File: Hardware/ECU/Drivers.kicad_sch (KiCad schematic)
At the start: 52 parts, among them SW4 SW_DPDT_x2, U10 TC4424A, U5 TC4424A, U6 TC4424A, U7 MC33810, U8 MC33810, U9 TC4424A

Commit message: PCB
Platine Vernetzt
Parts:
- removed D10, D12, D14, D16: D, Diode_SMD:D_SOD-323, symbol Device:D
- removed D17, D20, D23, D24, D3, D4, D6, D8: LED, LED_SMD:LED_0805_2012Metric, symbol Device:LED
- removed R11, R12, R14, R16, R19, R22, R25, R26: 1k, Resistor_SMD:R_0805_2012Metric, symbol Device:R
- removed R18: 10k, Resistor_SMD:R_0805_2012Metric, symbol Device:R
- removed U10, U6: TC4424A, Package_SO:SOIC-8_3.9x4.9mm_P1.27mm, symbol IC_Automotive:TC4424A
- removed U8: MC33810, IC_Automotive:SOIC32-P0.65-33N, symbol IC_Automotive:MC33810
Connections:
- net 12V-SW: now also R13.2; no longer R13.1
- net at D5.2 (A): now also R13.1; no longer R13.2
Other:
- moved on the sheet: R13

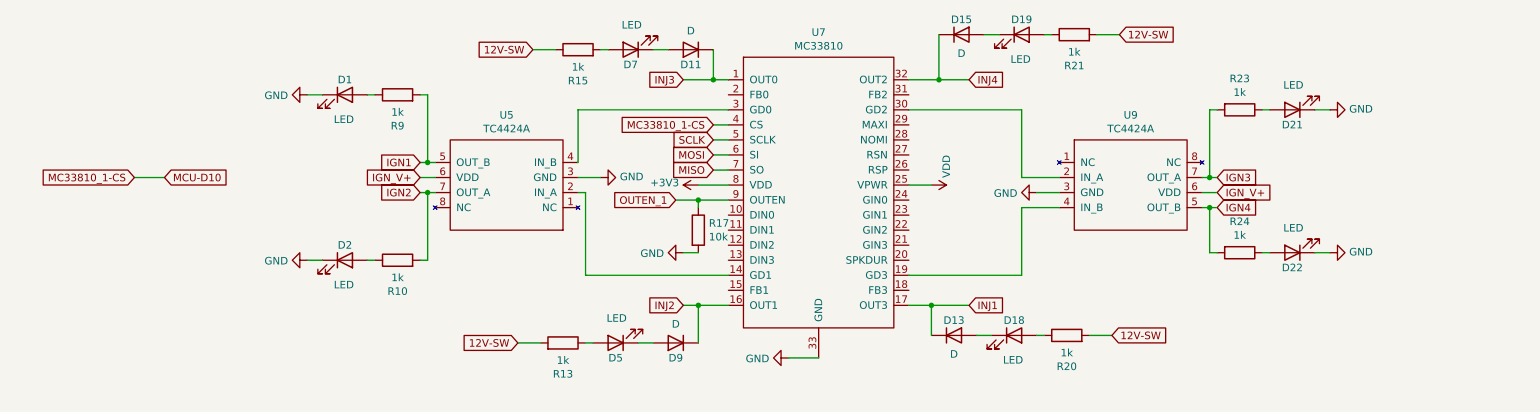
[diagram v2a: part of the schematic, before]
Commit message: Add new footprint for TO-220AB MOSFET (IRFB4110PBF)
- Created a new KiCad module for the TO254P483X1016X1994-3P footprint.
- Included necessary graphical elements such as courtyard, fabrication, and silkscreen layers.
- Defined pads for through-hole connections with appropriate dimensions and drill sizes.
- Added a 3D model reference for the IRFB4110PBF component.
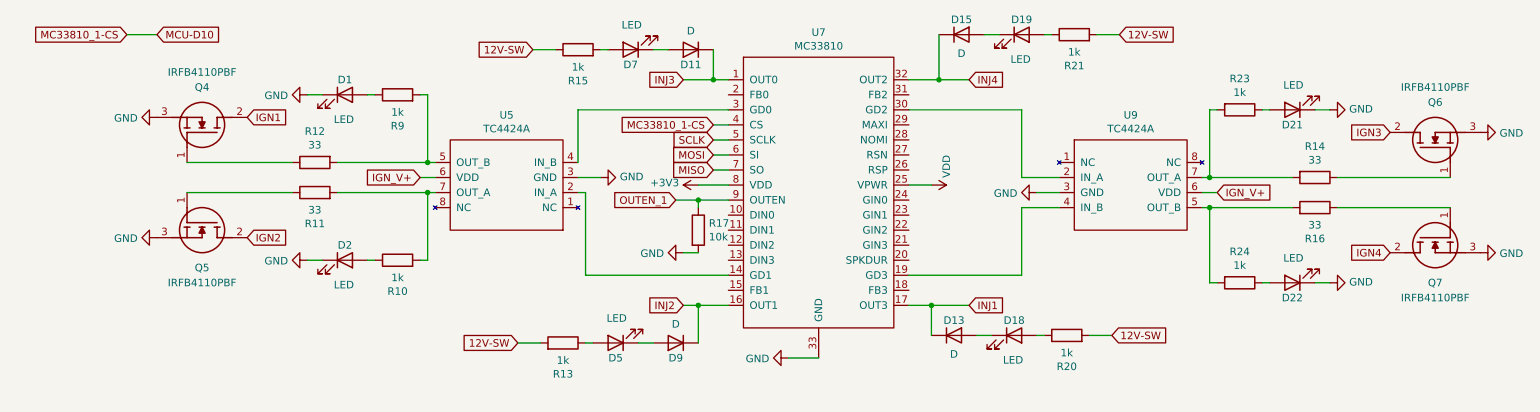
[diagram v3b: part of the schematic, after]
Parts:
- added Q4, Q5, Q6, Q7: IRFB4110PBF, TO254P483X1016X1994-3P, symbol LIB_IRFB4110PBF:IRFB4110PBF
- added R11, R12, R14, R16: 33, Resistor_SMD:R_0805_2012Metric, symbol Device:R
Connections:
- net GND: now also Q4.3 (S), Q5.3 (S), Q6.3 (S), Q7.3 (S)
- net IGN1: now also Q4.2 (D); no longer R9.2, U5.5 (OUT_B)
- net IGN2: now also Q5.2 (D); no longer R10.2, U5.7 (OUT_A)
- net IGN3: now also Q6.2 (D); no longer R23.2, U9.7 (OUT_A)
- net IGN4: now also Q7.2 (D); no longer R24.2, U9.5 (OUT_B)
- new net: R12.2, R9.2, U5.5 (OUT_B)
- new net: Q5.1 (G), R11.1
- new net: Q7.1 (G), R16.1
- new net: R16.2, R24.2, U9.5 (OUT_B)
- new net: R14.2, R23.2, U9.7 (OUT_A)
- new net: R10.2, R11.2, U5.7 (OUT_A)
- new net: Q4.1 (G), R12.1
- new net: Q6.1 (G), R14.1
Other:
- moved on the sheet: D22, R24

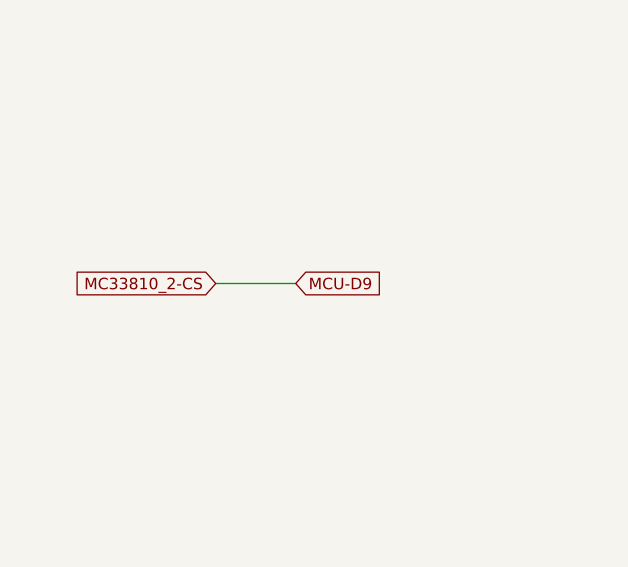
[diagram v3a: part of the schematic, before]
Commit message: modified:   Hardware/ECU/Drivers.kicad_sch 	deleted:    Hardware/ECU/ECU-backups/ECU-2025-05-15_143348.zip 	deleted:    Hardware/ECU/ECU-backups/ECU-2025-05-15_144355.zip 	deleted:    Hardware/ECU/ECU-backups/ECU-2025-05-15_152109.zip 	deleted:    Hardware/ECU/ECU-backups/ECU-2025-05-15_161628.zip 	deleted:    Hardware/ECU/ECU-backups/ECU-2025-05-15_162311.zip 	deleted:    Hardware/ECU/ECU-backups/ECU-2025-05-16_191516.zip 	deleted:    Hardware/ECU/ECU-backups/ECU-2025-05-16_192518.zip 	deleted:    Hardware/ECU/ECU-backups/ECU-2025-05-16_193610.zip 	new file:   Hardware/ECU/ECU-backups/ECU-2025-05-20_084251.zip 	new file:   Hardware/ECU/ECU-backups/ECU-2025-05-20_085713.zip 	new file:   Hardware/ECU/ECU-backups/ECU-2025-05-20_090304.zip 	new file:   Hardware/ECU/ECU-backups/ECU-2025-05-20_142748.zip 	new file:   Hardware/ECU/ECU-backups/ECU-2025-05-20_150003.zip 	new file:   Hardware/ECU/ECU-backups/ECU-2025-05-27_131057.zip 	new file:   Hardware/ECU/ECU-backups/ECU-2025-05-27_141528.zip 	new file:   Hardware/ECU/ECU-backups/ECU-2025-05-27_154948.zip 	new file:   Hardware/ECU/ECU-backups/ECU-2025-05-27_155558.zip 	new file:   Hardware/ECU/ECU.csv 	modified:   Hardware/ECU/ECU.kicad_pcb 	modified:   Hardware/ECU/ECU.kicad_pcb.zip 	new file:   Hardware/ECU/ECU.xml 	modified:   Hardware/ECU/Power-Regulator.kicad_sch 	modified:   Hardware/ECU/docs/Pinout.ods 	modified:   Hardware/ECU/fp-info-cache 	modified:   Hardware/ECU/fp-lib-table 	new file:   Hardware/ECU/lib/CRCW060349K9FKEAC.step 	new file:   Hardware/ECU/lib/CRCW060349K9FKEAC.wrl 	new file:   Hardware/ECU/lib/GRM21BC81A226ME44L.step 	new file:   Hardware/ECU/lib/GRM21BC81A226ME44L.wrl 	new file:   Hardware/ECU/lib/SamacSys_Parts.3dshapes/NE555DR.stp 	new file:   Hardware/ECU/lib/SamacSys_Parts.dcm 	new file:   Hardware/ECU/lib/SamacSys_Parts.kicad_sym 	new file:   Hardware/ECU/lib/SamacSys_Parts.lib 	new file:   Hardware/ECU/lib/SamacSys_Parts.mod 	new file:   Hardware/ECU/lib/SamacSys_Parts.pretty/NE555DR.kica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
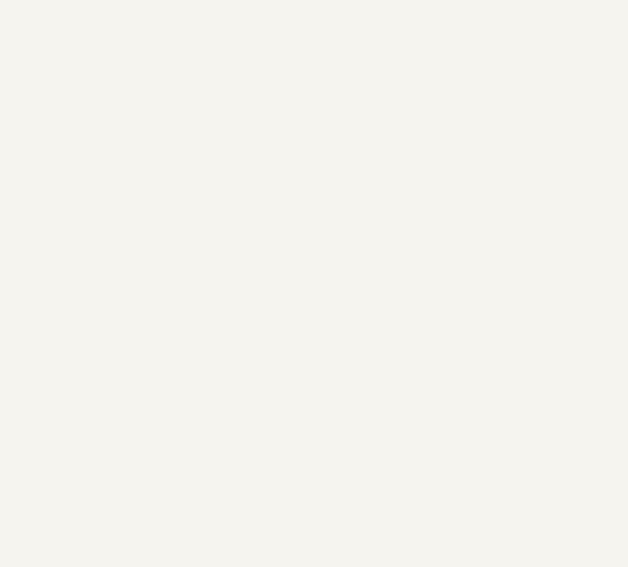
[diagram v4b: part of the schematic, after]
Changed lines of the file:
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@@
-	(wire
-		(pts
-			(xy 50.8 116.84) (xy 41.91 116.84)
-		)
-		(stroke
-			(width 0)
-			(type default)
-		)
-	)
 	(wire
 		(pts
@@
 		)
 	)
-	(global_label "MC33810_2-CS"
-		(shape input)
-		(at 41.91 116.84 180)
-		(fields_autoplaced yes)
-		(effects
-			(font
-				(size 1.27 1.27)
-			)
-			(justify right)
-		)
-		(property "Intersheetrefs" "${INTERSHEET_REFS}"
-			(at 24.6605 116.84 0)
-			(effects
-				(font
-					(size 1.27 1.27)
-				)
-				(justify right)
-				(hide yes)
-			)
-		)
-	)
 	(global_label "12V-SW"
 		(shape input)
@@
 			(effects
 				(font
-					(size 1.27 1.27)
-				)
-				(justify left)
-				(hide yes)
-			)
-		)
-	)
-	(global_label "MCU-D9"
-		(shape input)
-		(at 50.8 116.84 0)
-		(fields_autoplaced yes)
-		(effects
-			(font
-				(size 1.27 1.27)
-			)
-			(justify left)
-		)
-		(property "Intersheetrefs" "${INTERSHEET_REFS}"
-			(at 61.1554 116.84 0)
-			(effects
-				(font

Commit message: modified:   Hardware/ECU/Drivers.kicad_sch 	deleted:    Hardware/ECU/ECU-backups/ECU-2025-05-27_180718.zip 	new file:   Hardware/ECU/ECU-backups/ECU-2025-08-25_112034.zip
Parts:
- R11, R12, R14, R16: Digikey Part Number 311-1.00KCRCT-ND -> RC0805FR-7W33RL; Manufacturer_Part_Number RC0805FR-071KL -> RC0805FR-7W33RL; URL https://www.digikey.com/product-detail/en/yageo/RC0805FR-07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 -> https://www.digikey.de/de/products/detail/yageo/RC0805FR-7W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
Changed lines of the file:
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@@
 			)
 		)
-		(property "Digikey Part Number" "311-1.00KCRCT-ND"
+		(property "Digikey Part Number" "RC0805FR-7W33RL"
 			(at 240.03 48.26 0)
 			(effects
@@
 			)
 		)
-		(property "Manufacturer_Part_Number" "RC0805FR-071KL"
+		(property "Manufacturer_Part_Number" "RC0805FR-7W33RL"
 			(at 240.03 48.26 0)
 			(effects
@@
 			)
 		)
-		(property "URL" "https://www.digikey.com/product-detail/en/yageo/RC0805FR-071KL/311-1.00KCRCT-ND/730391"
+		(property "URL" "https://www.digikey.de/de/products/detail/yageo/RC0805FR-7W33RL/17023320"
 			(at 240.03 48.26 0)
 			(effects
@@
 			)
 		)
-		(property "Digikey Part Number" "311-1.00KCRCT-ND"
+		(property "Digikey Part Number" "RC0805FR-7W33RL"
 			(at 71.12 45.72 0)
 			(effects
@@
 			)
 		)
-		(property "Manufacturer_Part_Number" "RC0805FR-071KL"
+		(property "Manufacturer_Part_Number" "RC0805FR-7W33RL"
 			(at 71.12 45.72 0)
 			(effects
@@
 			)
 		)
-		(property "URL" "https://www.digikey.com/product-detail/en/yageo/RC0805FR-071KL/311-1.00KCRCT-ND/730391"
+		(property "URL" "https://www.digikey.de/de/products/detail/yageo/RC0805FR-7W33RL/17023320"
 			(at 71.12 45.72 0)
 			(effects
@@
 			)
 		)
-		(property "Digikey Part Number" "311-1.00KCRCT-ND"
+		(property "Digikey Part Number" "RC0805FR-7W33RL"
 			(at 71.12 40.64 0)
 			(effects
@@
 			)
 		)
-		(property "Manufacturer_Part_Number" "RC0805FR-071KL"
+		(property "Manufacturer_Part_Number" "RC0805FR-7W33RL"
 			(at 71.12 40.64 0)
 			(effects
@@
 			)
 		)
-		(property "URL" "https://www.digikey.com/product-detail/en/yageo/RC0805FR-071KL/311-1.00KCRCT-ND/730391"
+		(property "URL" "https://www.digikey.de/de/products/detail/yageo/RC0805FR-7W33RL/17023320"
 			(at 71.12 40.64 0)
 			(effects
@@
 			)
 		)
-		(property "Digikey Part Number" "311-1.00KCRCT-ND"
+		(property "Digikey Part Number" "RC0805FR-7W33RL"
 			(at 240.03 43.18 0)
 			(effects
@@
 			)
 		)
-		(property "Manufacturer_Part_Number" "RC0805FR-071KL"
+		(property "Manufacturer_Part_Number" "RC0805FR-7W33RL"
 			(at 240.03 43.18 0)
 			(effects
@@
 			)
 		)
-		(property "URL" "https://www.digikey.com/product-detail/en/yageo/RC0805FR-071KL/311-1.00KCRCT-ND/730391"
+		(property "URL" "https://www.digikey.de/de/products/detail/yageo/RC0805FR-7W33RL/17023320"
 			(at 240.03 43.18 0)
 			(effects
